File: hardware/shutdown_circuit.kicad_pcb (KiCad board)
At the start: 2 copper layers, 56.5 x 65 mm, 4 parts

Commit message: PILOT Drive HAT MKII
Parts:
- added BT1: BLP2032SM-GTR, pilot_footprints:RTC_Battery_Holder, F.Cu at (106.5, 125.8)
- added C1: 1000uF, pilot_footprints:1000uF_10v, F.Cu at (91.6, 141.5)
- added C2: 100uF, pilot_footprints:100uF_35v, F.Cu at (87.9, 110.3)
- added C3: 100nF, Capacitor_SMD:C_0402_1005Metric_Pad0.74x0.62mm_HandSolder, F.Cu at (103.6, 108.8)
- added C4: 10uF, Capacitor_SMD:C_0402_1005Metric_Pad0.74x0.62mm_HandSolder, F.Cu at (103.6, 107.7)
- added D1: SMLJ60S10, Diode_SMD:D_SMC_Handsoldering, F.Cu at (78.8, 104.8)
- added D10: RB520S30T1G, pilot_footprints:3v3_TVS, F.Cu at (100.5, 106.2)
- added D11: RB520S30T1G, pilot_footprints:3v3_TVS, F.Cu at (95.6, 98.3)
- added D12: RB520S30T1G, pilot_footprints:3v3_TVS, F.Cu at (86.9, 99.2)
- added D2: ESD12VD3B, Diode_SMD:D_SOD-323, F.Cu at (69.2, 95.1)
- added D3: SMLJ60S10, Diode_SMD:D_SMC_Handsoldering, F.Cu at (71.9, 104.8)
- added D4: CDSOD323-T15S, Diode_SMD:D_SOD-323F, F.Cu at (83.2, 112.7)
- added D5: B340LB-13-F, Diode_SMD:D_SMC_Handsoldering, F.Cu at (89.1, 126.8)
- added D6: R_LED, LED_SMD:LED_0603_1608Metric_Pad1.05x0.95mm_HandSolder, F.Cu at (115.5, 95.0)
- added D7: RB520S30T1G, pilot_footprints:3v3_TVS, F.Cu at (94.1, 113.9)
- added D8: RB520S30T1G, pilot_footprints:3v3_TVS, F.Cu at (94.1, 106.3)
- added D9: G_LED, LED_SMD:LED_0603_1608Metric_Pad1.05x0.95mm_HandSolder, F.Cu at (115.4, 100.0)
- added F1: 3414.0124.26, Fuse:Fuse_0402_1005Metric_Pad0.77x0.64mm_HandSolder, F.Cu at (76.6, 97.3)
- added F2: 3414.0124.26, Fuse:Fuse_0402_1005Metric_Pad0.77x0.64mm_HandSolder, F.Cu at (74.2, 97.3)
- added G***: LOGO, pilot_footprints:oshw_logo, F.Cu at (110.6, 101.0)
- added G***: LOGO, pilot_footprints:lamemakes_logo, F.Cu at (104.2, 145.1)
- added J1: 284391-7, pilot_footprints:Screw_Term, F.Cu at (72.5, 92.3)
- added J2: Raspberry_Pi_4, Connector_PinSocket_2.54mm:PinSocket_2x20_P2.54mm_Vertical, B.Cu at (65.0, 118.4)
- added J3: 6W Header, Connector_PinHeader_2.54mm:PinHeader_1x06_P2.54mm_Vertical, F.Cu at (111.7, 139.7)
- added J4: 6W Header, Connector_PinHeader_2.54mm:PinHeader_1x06_P2.54mm_Vertical, F.Cu at (100.7, 103.6)
- added L1: 100uH, pilot_footprints:100uH_Inductor, F.Cu at (78.3, 143.0)
- added Q1: DMN63D8L-7, pilot_footprints:N_FET, F.Cu at (87.5, 117.6)
- added Q2: IRF9540N, pilot_footprints:P_FET, F.Cu at (73.6, 118.3)
- added R1: 10k, Resistor_SMD:R_0402_1005Metric_Pad0.72x0.64mm_HandSolder, F.Cu at (69.7, 97.3)
- added R10: 4k7, Resistor_SMD:R_0402_1005Metric_Pad0.72x0.64mm_HandSolder, F.Cu at (72.9, 112.3)
- added R11: 4k7, Resistor_SMD:R_0402_1005Metric_Pad0.72x0.64mm_HandSolder, F.Cu at (76.1, 112.3)
- added R13: 4k7, Resistor_SMD:R_0402_1005Metric_Pad0.72x0.64mm_HandSolder, F.Cu at (68.9, 140.3)
- added R14: 4k7, Resistor_SMD:R_0402_1005Metric_Pad0.72x0.64mm_HandSolder, F.Cu at (68.9, 137.9)
- added R15: 1k, Resistor_SMD:R_0402_1005Metric_Pad0.72x0.64mm_HandSolder, F.Cu at (83.7, 105.4)
- added R16: 4k7, Resistor_SMD:R_0402_1005Metric_Pad0.72x0.64mm_HandSolder, F.Cu at (69.5, 150.0)
- added R2: 22k, Resistor_SMD:R_0402_1005Metric_Pad0.72x0.64mm_HandSolder, F.Cu at (94.1, 115.2)
- added R3: 10k, Resistor_SMD:R_0402_1005Metric_Pad0.72x0.64mm_HandSolder, F.Cu at (80.0, 113.8)
- added R4: 1k, Resistor_SMD:R_0402_1005Metric_Pad0.72x0.64mm_HandSolder, F.Cu at (104.4, 100.3)
- added R5: 4k7, Resistor_SMD:R_0402_1005Metric_Pad0.72x0.64mm_HandSolder, F.Cu at (104.4, 87.0)
- added R6: 1k, Resistor_SMD:R_0402_1005Metric_Pad0.72x0.64mm_HandSolder, F.Cu at (97.6, 100.3)
- added R7: 330, Resistor_SMD:R_0402_1005Metric_Pad0.72x0.64mm_HandSolder, F.Cu at (114.1, 95.6)
- added R8: 4k7, Resistor_SMD:R_0402_1005Metric_Pad0.72x0.64mm_HandSolder, F.Cu at (97.6, 87.0)
- added R9: 100, Resistor_SMD:R_0402_1005Metric_Pad0.72x0.64mm_HandSolder, F.Cu at (114.0, 100.5)
- added U1: SFH617A-1X007T, pilot_footprints:Optocoupler, F.Cu at (106.0, 93.6)
- added U2: LM2576HVS-3.3, Package_TO_SOT_SMD:TO-263-5_TabPin3, F.Cu at (76.7, 129.6)
- added U3: DS1307+, pilot_footprints:DS1307Z+T&R, F.Cu at (113.8, 110.2)
- added U4: SFH617A-1X007T, pilot_footprints:Optocoupler, F.Cu at (99.2, 93.6)
- added U5: ATtiny85-20SUR, pilot_footprints:ATTINY_SUR, F.Cu at (97.6, 110.1)
- added U6: CAT24C128, pilot_footprints:CAT24C128YI, F.Cu at (84.1, 101.1)
- added Y1: 32.768 kHz, pilot_footprints:RTC_Crystal, F.Cu at (108.6, 109.8)
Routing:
- net /+3v3: track 0.00 -> 170.8 mm, vias 0 -> 6
- net /+5v: track 0.00 -> 144.5 mm, vias 0 -> 6
- net /BACKUP_BTN: track 0.00 -> 97.8 mm, vias 0 -> 4
- net /MOSI: track 0.00 -> 97.4 mm, vias 0 -> 6
- net /SCL: track 0.00 -> 94.3 mm, vias 0 -> 5
- net /HL_Opto: track 0.00 -> 75.1 mm, vias 0 -> 1
- net Net-(D11-Pad2): track 0.00 -> 62.2 mm, vias 0 -> 3
- net GND: track 0.00 -> 62.0 mm, vias 0 -> 48
- net /MISO: track 0.00 -> 54.3 mm, vias 0 -> 2
- net /+12v_OUT: track 0.00 -> 52.6 mm, vias 0 -> 3
- net /ID_SDA: track 0.00 -> 44.1 mm, vias 0 -> 4
- net /FET_CTRL: track 0.00 -> 44.0 mm, vias 0 -> 2
- net /ID_SCL: track 0.00 -> 43.7 mm, vias 0 -> 5
- net /ATTINY_VCC: track 0.00 -> 43.3 mm, vias 0 -> 1
- net /+12v_ACC: track 0.00 -> 41.5 mm
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- added copper zone on B.Cu, net GND
- added copper zone on F.Cu, net GND
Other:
- board text added: "MK II"
- board text added: "PILOT Drive HAT"
- board text added: "PWR"
- board text added: "STAT"

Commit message: Post-MKII Prototype fixes
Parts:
- removed the G*** at (110.6, 101.0)
- added G***: LOGO, pilot_footprints:arrow, F.Cu at (105.5, 134.6)
- added G***: LOGO, pilot_footprints:arrow, F.Cu at (103.1, 101.7)
- added REF**: OSHW-Symbol_6.7x6mm_SilkScreen, Symbol:OSHW-Symbol_6.7x6mm_SilkScreen, F.Cu at (101.3, 142.5)
- moved G*** 7.25 mm to (110.8, 142.0)
- moved D10 3.44 mm to (97.0, 106.2)
- moved R4 2.74 mm to (102.7, 98.1), turned to -90 degrees
- moved R6 2.71 mm to (96.0, 98.1), turned to -90 degrees
- moved D11 2.28 mm to (93.5, 97.5), turned to 180 degrees
- moved J3 1.89 mm to (111.8, 137.8)
- moved J4 1.88 mm to (100.7, 101.7)
- moved BT1 1.76 mm to (106.5, 124.0)
- moved D12 0.81 mm to (86.8, 98.4)
- turned D9 to 90 degrees
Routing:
- net Net-(D5-Pad1): track 16.2 -> 23.3 mm
- net GND: track 62.0 -> 68.1 mm, vias 48 -> 47
- net Net-(J4-Pad1): track 33.0 -> 27.7 mm, vias 3 -> 1
- net /MISO: track 54.3 -> 57.8 mm
- net /+12v_HL: track 29.8 -> 26.4 mm
- net /ID_SCL: track 43.7 -> 47.1 mm
- net /+5v: track 144.5 -> 147.2 mm
- net /+12v_ACC: track 41.5 -> 39.1 mm
- net /RTC_Bat: track 30.8 -> 28.5 mm
- net Net-(D12-Pad1): track 9.83 -> 12.0 mm
- net /ATTINY_VCC: track 43.3 -> 45.5 mm
- net /RESET: track 36.3 -> 34.3 mm
- net /ID_SDA: track 44.1 -> 46.0 mm, vias 4 -> 5
- net /MOSI: track 97.4 -> 99.3 mm, vias 6 -> 4
- net Net-(D11-Pad2): track 62.2 -> 60.6 mm
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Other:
- outline, holes or cut-outs redrawn
- board text added: "ATTiny85 Program/Debug"
- board text added: "GND"
- board text added: "ID EEPROM Program/Debug"
- board text added: "MOSI"
- board text added: "RST"
- board text added: "SCL"
- board text added: "SDA"
- board text added: "VCC"
- board text added: "WP"

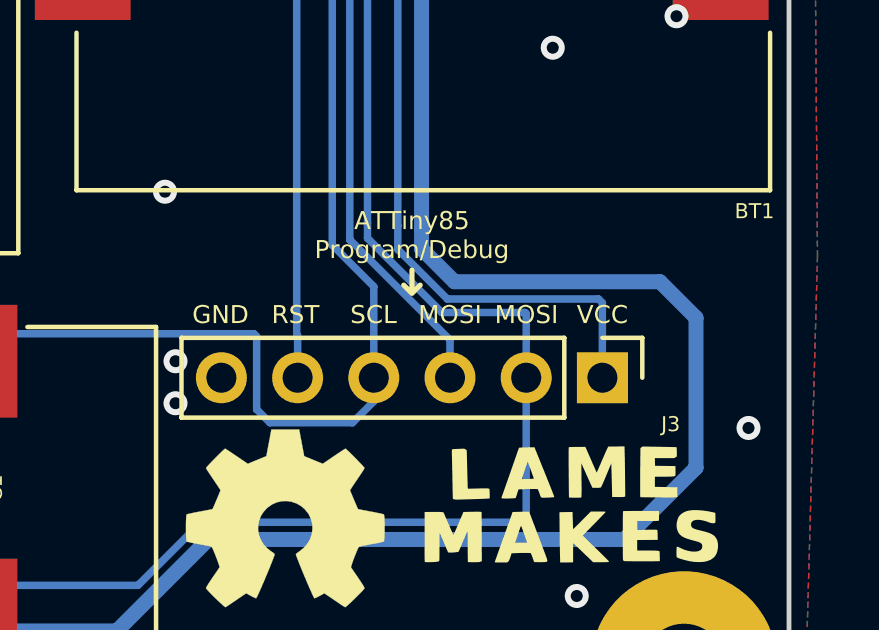
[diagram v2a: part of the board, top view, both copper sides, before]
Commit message: PCB Typo fixes
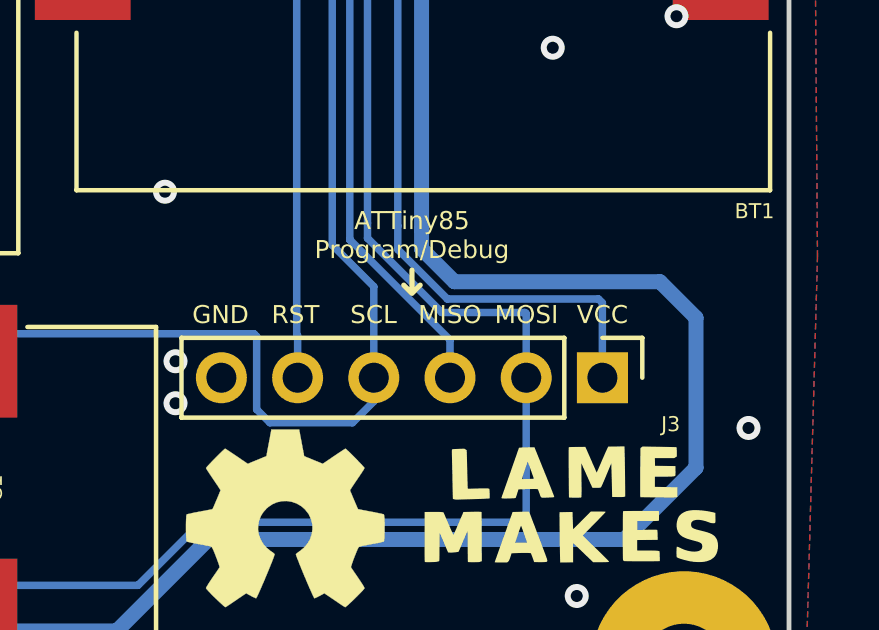
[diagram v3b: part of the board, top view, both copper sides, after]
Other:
- board text added: "MISO"
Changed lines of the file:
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@@
     (effects (font (size 0.6 0.6) (thickness 0.15)))
   )
-  (gr_text "MOSI" (at 106.7644 135.6996) (layer "F.SilkS")
+  (gr_text "MISO" (at 106.7644 135.6996) (layer "F.SilkS")
     (effects (font (size 0.6 0.6) (thickness 0.15)))
   )

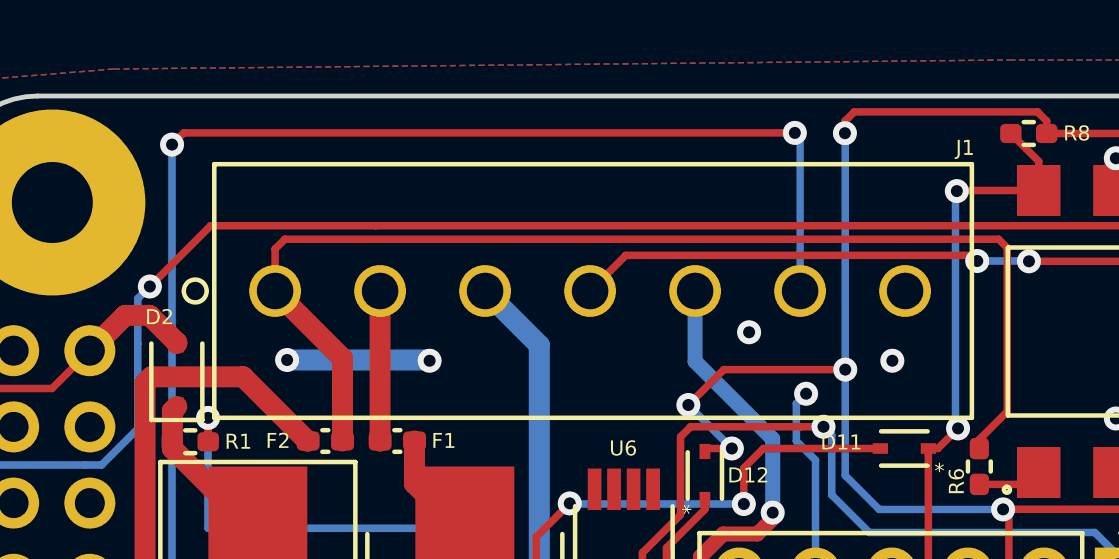
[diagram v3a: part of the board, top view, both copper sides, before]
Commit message: README RTC updates
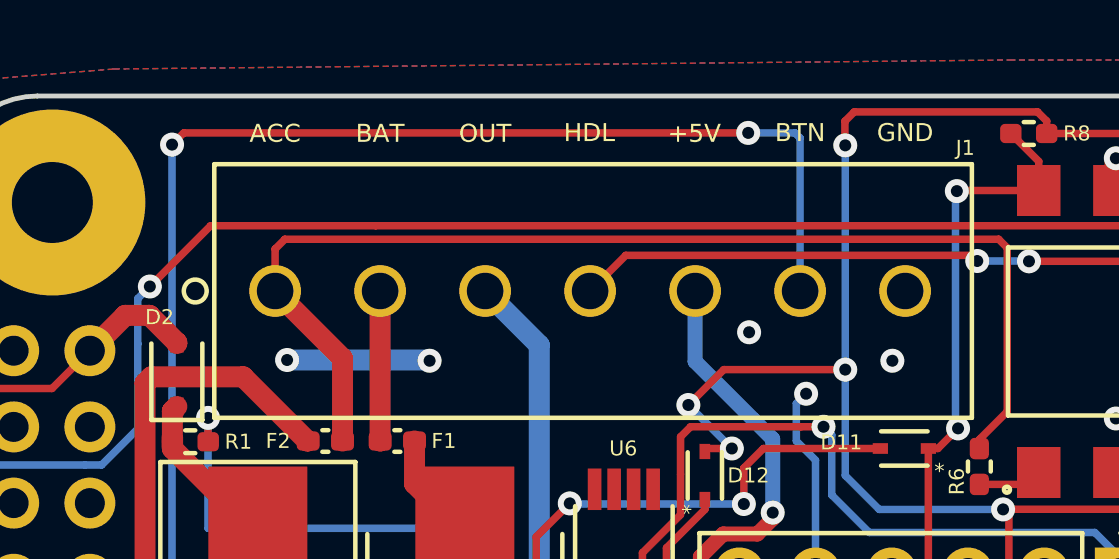
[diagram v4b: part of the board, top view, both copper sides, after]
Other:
- board text added: "+5V"
- board text added: "ACC"
- board text added: "BAT"
- board text added: "BTN"
- board text added: "HDL"
- board text added: "OUT"
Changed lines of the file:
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@@
   (gr_arc locked (start 64.5644 150.7996) (mid 62.44308 149.92092) (end 61.5644 147.7996) (layer "Edge.Cuts") (width 0.16))
   (gr_arc locked (start 115.0644 85.7996) (mid 117.18572 86.67828) (end 118.0644 88.7996) (layer "Edge.Cuts") (width 0.16))
+  (gr_text "OUT" (at 79.4894 87.0496) (layer "F.SilkS")
+    (effects (font (size 0.6 0.6) (thickness 0.15)))
+  )
+  (gr_text "BTN" (at 89.9894 87.0246) (layer "F.SilkS")
+    (effects (font (size 0.6 0.6) (thickness 0.15)))
+  )
   (gr_text "ID EEPROM\nProgram/Debug" (at 103.8144 101.6996) (layer "F.SilkS")
     (effects (font (size 0.6 0.6) (thickness 0.15)) (justify left))
@@
     (effects (font (size 0.6 0.6) (thickness 0.15)))
   )
+  (gr_text "BAT" (at 75.9894 87.0496) (layer "F.SilkS")
+    (effects (font (size 0.6 0.6) (thickness 0.15)))
+  )
   (gr_text "PWR" (at 117.1344 95.0296 90) (layer "F.SilkS")
     (effects (font (size 0.75 0.75) (thickness 0.1875)))
@@
     (effects (font (size 0.75 0.75) (thickness 0.1875)))
   )
+  (gr_text "ACC" (at 72.4894 87.0496) (layer "F.SilkS")
+    (effects (font (size 0.6 0.6) (thickness 0.15)))
+  )
   (gr_text "VCC\n" (at 111.8444 135.6996) (layer "F.SilkS")
+    (effects (font (size 0.6 0.6) (thickness 0.15)))
+  )
+  (gr_text "HDL" (at 82.9644 87.0246) (layer "F.SilkS")
+    (effects (font (size 0.6 0.6) (thickness 0.15)))
+  )
+  (gr_text "GND" (at 93.4894 87.0246) (layer "F.SilkS")
+    (effects (font (size 0.6 0.6) (thickness 0.15)))
+  )
+  (gr_text "+5V" (at 86.4644 87.0496) (layer "F.SilkS")
     (effects (font (size 0.6 0.6) (thickness 0.15)))
   )
@@
   (segment (start 79.0694 127.8746) (end 82.4894 127.8746) (width 0.25) (layer "F.Cu") (net 2))
   (segment (start 79.5744 142.9996) (end 72.427 142.9996) (width 0.25) (layer "F.Cu") (net 2))
+  (segment (start 91.4844 86.6396) (end 91.4844 87.4346) (width 0.25) (layer "F.Cu") (net 2))
   (segment (start 68.9444 138.4496) (end 69.9244 138.4496) (width 0.25) (layer "F.Cu") (net 2))
   (segment (start 96.9494 99.773291) (end 96.9494 102.8596) (width 0.25) (layer "F.Cu") (net 2))
@@
   (segment (start 96.2143 105.5497) (end 96.2143 106.2496) (width 0.25) (layer "F.Cu") (net 2))
   (segment (start 96.2143 107.0255) (end 96.9264 107.7376) (width 0.25) (layer "F.Cu") (net 2))
+  (segment (start 91.4844 87.4346) (end 91.4944 87.4446) (width 0.25) (layer "F.Cu") (net 2))
   (segment (start 73.4994 112.2796) (end 73.4994 112.0746) (width 0.25) (layer "F.Cu") (net 2))
   (segment (start 77.016998 112.594698) (end 76.7019 112.2796) (width 0.25) (layer "F.Cu") (net 2))
   (segment (start 96.3094 103.4996) (end 96.3094 105.4546) (width 0.25) (layer "F.Cu") (net 2))
   (segment (start 73.4994 112.0746) (end 74.1144 111.4596) (width 0.25) (layer "F.Cu") (net 2))
-  (segment (start 91.4844 87.0396) (end 91.4844 86.6396) (width 0.25) (layer "F.Cu") (net 2))
   (segment (start 79.8648 143.2896) (end 79.8644 143.2896) (width 0.25) (layer "F.Cu") (net 2))
   (segment (start 86.9143 97.5496) (end 86.8144 97.6495) (width 0.25) (layer "F.Cu") (net 2))
@@
   (via (at 78.7144 128.2296) (size 0.8) (drill 0.4) (layers "F.Cu" "B.Cu") (net 2))
   (via (at 87.7144 97.5496) (size 0.8) (drill 0.4) (layers "F.Cu" "B.Cu") (net 2))
-  (via (at 91.4844 87.0396) (size 0.8) (drill 0.4) (layers "F.Cu" "B.Cu") (net 2))
   (via (at 86.2644 96.0996) (size 0.8) (drill 0.4) (layers "F.Cu" "B.Cu") (net 2))
   (via (at 96.75575 99.579641) (size 0.8) (drill 0.4) (layers "F.Cu" "B.Cu") (net 2))
   (via (at 91.4944 94.9196) (size 0.8) (drill 0.4) (layers "F.Cu" "B.Cu") (net 2))
+  (via (at 91.4944 87.4446) (size 0.8) (drill 0.4) (layers "F.Cu" "B.Cu") (net 2))
   (via (at 77.2044 112.594698) (size 0.8) (drill 0.4) (layers "F.Cu" "B.Cu") (net 2))
   (segment (start 91.4944 98.4496) (end 91.4944 94.9196) (width 0.25) (layer "B.Cu") (net 2))
@@
   (segment (start 71.2244 129.9296) (end 72.9244 128.2296) (width 0.25) (layer "B.Cu") (net 2))
   (segment (start 78.7144 113.3396) (end 78.7144 113.0996) (width 0.25) (layer "B.Cu") (net 2))
-  (segment (start 91.4944 94.9196) (end 91.4944 87.0496) (width 0.25) (layer "B.Cu") (net 2))
+  (segment (start 91.4944 94.9196) (end 91.4944 87.4446) (width 0.25) (layer "B.Cu") (net 2))
   (segment (start 87.727101 97.562301) (end 87.7144 97.5496) (width 0.25) (layer "B.Cu") (net 2))
-  (segment (start 91.4944 87.0496) (end 91.4844 87.0396) (width 0.25) (layer "B.Cu") (net 2))
   (segment (start 77.2044 112.594698) (end 78.209498 112.594698) (width 0.25) (layer "B.Cu") (net 2))
   (segment (start 87.727101 97.562301) (end 86.2644 96.0996) (width 0.25) (layer "B.Cu") (net 2))
@@
   (segment (start 86.489402 92.299599) (end 86.489402 94.646684) (width 0.5) (layer "B.Cu") (net 7))
   (segment (start 69.2404 146.2396) (end 95.6564 146.2396) (width 0.5) (layer "B.Cu") (net 7))
-  (segment (start 89.8144 87.0296) (end 69.4444 87.0296) (width 0.25) (layer "F.Cu") (net 8))
   (segment (start 69.4444 87.0296) (end 69.0544 87.4196) (width 0.25) (layer "F.Cu") (net 8))
+  (segment (start 88.2594 87.0296) (end 69.4444 87.0296) (width 0.25) (layer "F.Cu") (net 8))
   (segment (start 70.1319 144.584202) (end 70.1144 144.566702) (width 0.25) (layer "F.Cu") (net 8))
   (segment (start 68.039898 127.5496) (end 68.039898 129.274102) (width 0.25) (layer "F.Cu") (net 8))
@@
   (segment (start 70.1319 149.9896) (end 70.1319 144.584202) (width 0.25) (layer "F.Cu") (net 8))
   (via (at 70.1144 144.566702) (size 0.8) (drill 0.4) (layers "F.Cu" "B.Cu") (net 8))
-  (via (at 89.8144 87.0296) (size 0.8) (drill 0.4) (layers "F.Cu" "B.Cu") (net 8))
+  (via (at 88.2594 87.0296) (size 0.8) (drill 0.4) (layers "F.Cu" "B.Cu") (net 8))
   (via (at 69.0544 87.4196) (size 0.8) (drill 0.4) (layers "F.Cu" "B.Cu") (net 8))
   (via (at 68.039898 127.5496) (size 0.8) (drill 0.4) (layers "F.Cu" "B.Cu") (net 8))
@@
   (segment (start 70.5344 102.1596) (end 69.4044 102.1596) (width 0.25) (layer "B.Cu") (net 8))
   (segment (start 69.9644 129.8496) (end 66.3144 129.8496) (width 0.25) (layer "B.Cu") (net 8))
-  (segment (start 89.989403 87.204603) (end 89.8144 87.0296) (width 0.25) (layer "B.Cu") (net 8))
   (segment (start 70.1144 144.566702) (end 70.1144 129.9996) (width 0.25) (layer "B.Cu") (net 8))
+  (segment (start 89.8194 87.0296) (end 88.2594 87.0296) (width 0.25) (layer "B.Cu") (net 8))
   (segment (start 69.4044 102.1596) (end 69.0544 101.8096) (width 0.25) (layer "B.Cu") (net 8))
   (segment (start 71.4144 104.2596) (end 71.4144 103.0396) (width 0.25) (layer "B.Cu") (net 8))
   (segment (start 69.0544 101.8096) (end 69.0544 87.4196) (width 0.25) (layer "B.Cu") (net 8))
+  (segment (start 89.989403 87.199603) (end 89.8194 87.0296) (width 0.25) (layer "B.Cu") (net 8))
   (segment (start 69.0544 126.535098) (end 68.039898 127.5496) (width 0.25) (layer "B.Cu") (net 8))
-  (segment (start 89.989403 92.299599) (end 89.989403 87.204603) (width 0.25) (layer "B.Cu") (net 8))
   (segment (start 69.6594 104.6146) (end 71.0594 104.6146) (width 0.25) (layer "B.Cu") (net 8))
   (segment (start 70.1144 129.9996) (end 69.9644 129.8496) (width 0.25) (layer "B.Cu") (net 8))
@@
   (segment (start 69.0544 125.7796) (end 69.0544 126.535098) (width 0.25) (layer "B.Cu") (net 8))
   (segment (start 69.0544 105.2196) (end 69.6594 104.6146) (width 0.25) (layer "B.Cu") (net 8))
+  (segment (start 89.989403 92.299599) (end 89.989403 87.199603) (width 0.25) (layer "B.Cu") (net 8))
   (segment (start 87.9394 107.4163) (end 87.9394 106.9496) (width 0.7) (layer "F.Cu") (net 9))
   (segment (start 112.9394 108.5246) (end 113.1144 108.5246) (width 0.7) (layer "F.Cu") (net 9))
